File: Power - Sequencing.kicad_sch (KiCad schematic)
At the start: 0 parts

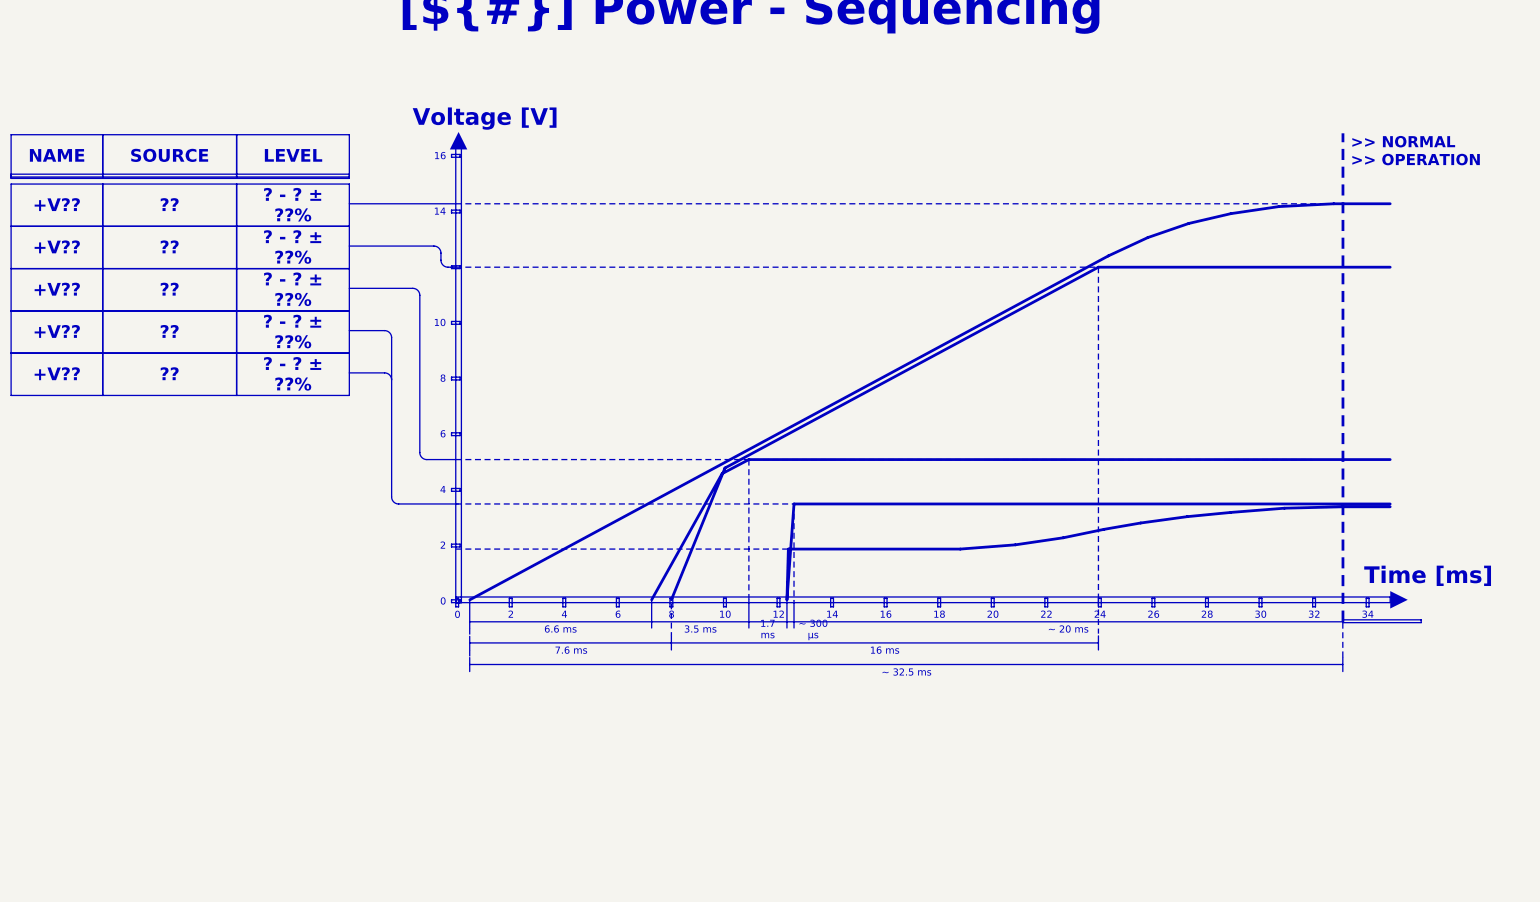
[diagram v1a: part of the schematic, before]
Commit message: Fill template pages: block diagram, power sequencing, cover notes, architecture
- Block Diagram redrawn from the real design: phase path (MR60PW, shunts),
  current and voltage channels with their gains and bandwidths, AD7606C-18,
  power chain, target specifications
- Power - Sequencing: start-up curves taken from the LTspice simulations
  (boost soft-start, analog rails) and rail table with sources, levels
  and timings
- Cover page: real design notes instead of the template examples
- Project Architecture: power-supply block documented, contiguous page
  numbers (Power Supply is page 6)
- Revision History: one column fed by the [Unreleased] changelog section
- sheet titles shortened so they fit the cover-page index: INA241 - Phase
  Sensing, Power Supply - Analog Rails

Sheet-level polylines carry no fill attribute (KiBot schematic reader).

Co-Authored-By: Claude Opus 5.5 <noreply@anthropic.com>
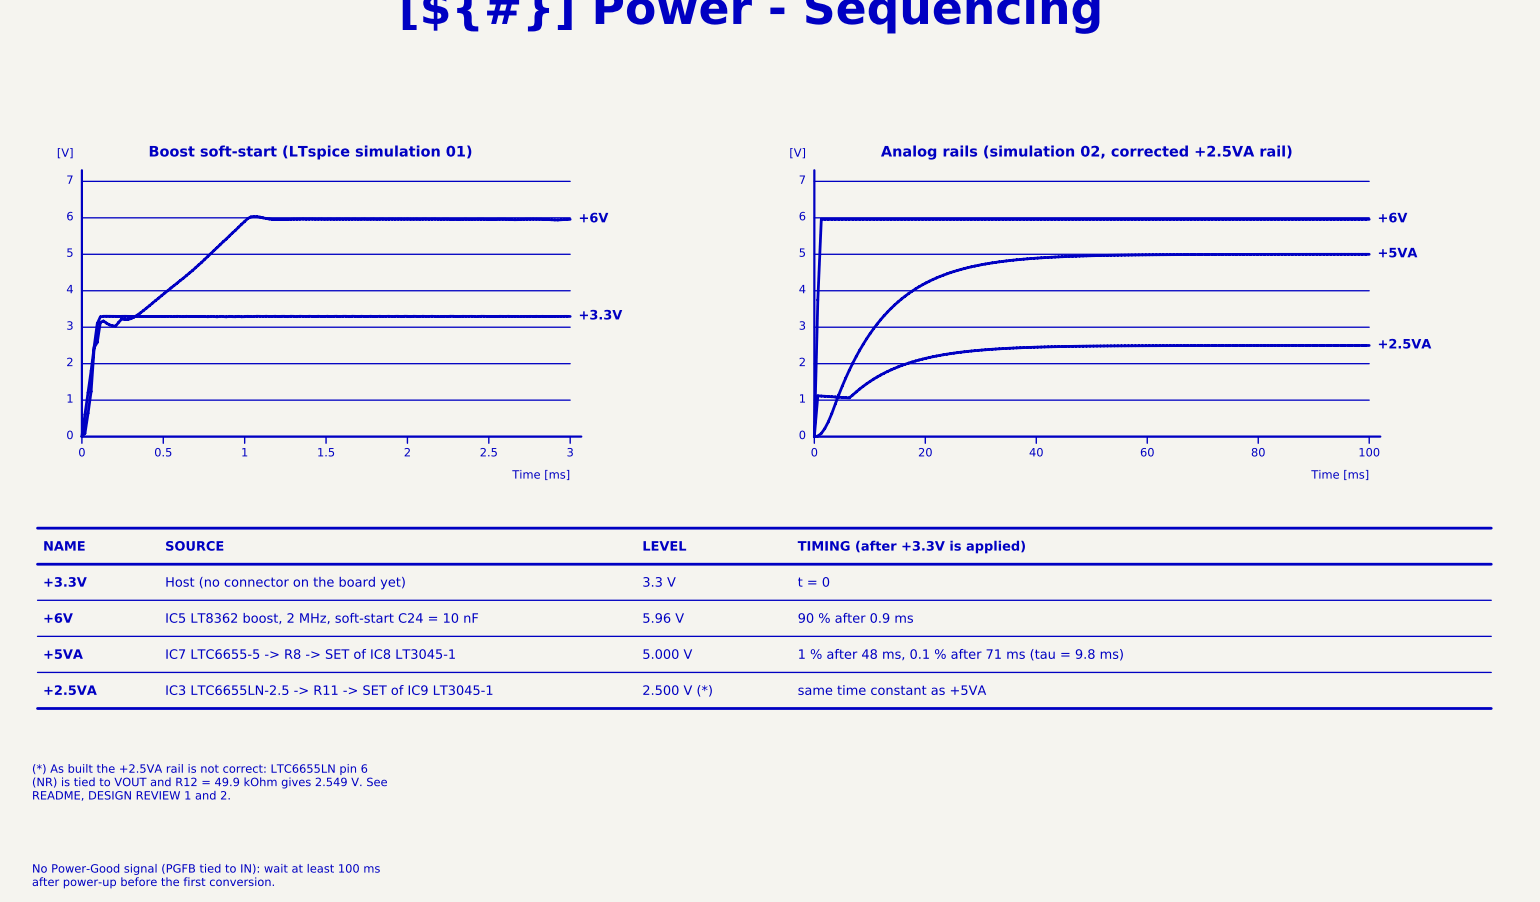
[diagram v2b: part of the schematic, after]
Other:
- note added: "+2.5VA"
- note added: "+3.3V"
- note added: "+5VA"
- note added: "+6V"
- note added: "0"
- note added: "0.5"
- note added: "1"
- note added: "1 % after 48 ms, 0.1 % after 71 ms (tau = 9.8 ms)"
- note added: "1.5"
- note added: "100"
- note added: "2"
- note added: "2.5"
- note added: "2.500 V (*)"
- note added: "20"
- note added: "3"
- note added: "3.3 V"
- note added: "4"
- note added: "40"
- note added: "5"
- note added: "5.000 V"
- note added: "5.96 V"
- note added: "6"
- note added: "60"
- note added: "7"
- note added: "80"
- note added: "90 % after 0.9 ms"
- note added: "Analog rails (simulation 02, corrected +2.5VA rail)"
- note added: "Boost soft-start (LTspice simulation 01)"
- note added: "Host (no connector on the board yet)"
- note added: "IC3 LTC6655LN-2.5 -> R11 -> SET of IC9 LT3045-1"
- note added: "IC5 LT8362 boost, 2 MHz, soft-start C24 = 10 nF"
- note added: "IC7 LTC6655-5 -> R8 -> SET of IC8 LT3045-1"
- note added: "LEVEL"
- note added: "NAME"
- note added: "SOURCE"
- note added: "TIMING (after +3.3V is applied)"
- note added: "[V]"
- note added: "same time constant as +5VA"
- note added: "t = 0"
- note removed: ">> NORMAL >> OPERATION"
- note removed: "Voltage [V]"

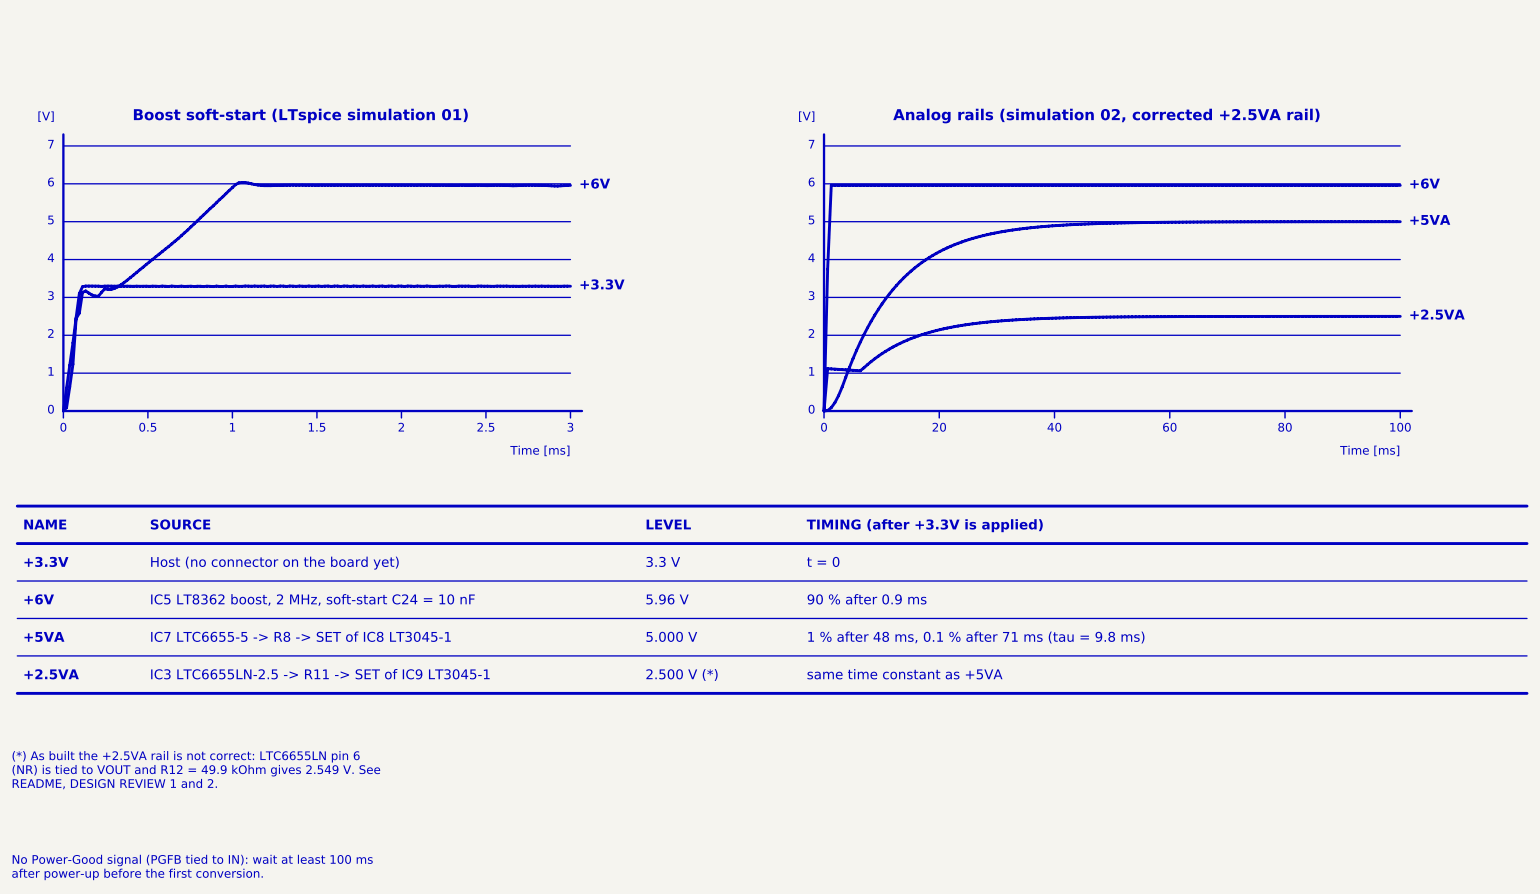
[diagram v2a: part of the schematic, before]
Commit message: Fix the +2.5VA reference, add XT60PW-M connectors, predict measurement quality
- IC3: LTC6655LN-2.5 replaced by the standard LTC6655-2.5, pin 6 is now
  VOUT_S tied to VOUT_F (the LN version has NR on that pin)
- R12: 49.9k -> 24.9k on the SET pin of IC9, +2.5VA = 2.500 V instead of
  2.549 V; both points removed from the README design review
- J5, J6: two Amass XT60PW-M added on the Connectors sheet and on the PCB,
  with symbol, footprint and 3D model in lib/. Their power pins are not
  wired yet
- Simulations 07 (ESC PWM waveforms through both channels) and 08 (Monte
  Carlo on the tolerances), analysed by measurement_quality.py into
  measurement_quality.md; plot style shared in plotstyle.py
- Simulations 01, 02, 04, results.md and their figures redone for the
  corrected rail
- README, README template and CHANGELOG updated; all sheets re-saved from
  KiCad

Co-Authored-By: Claude Opus 5.5 <noreply@anthropic.com>
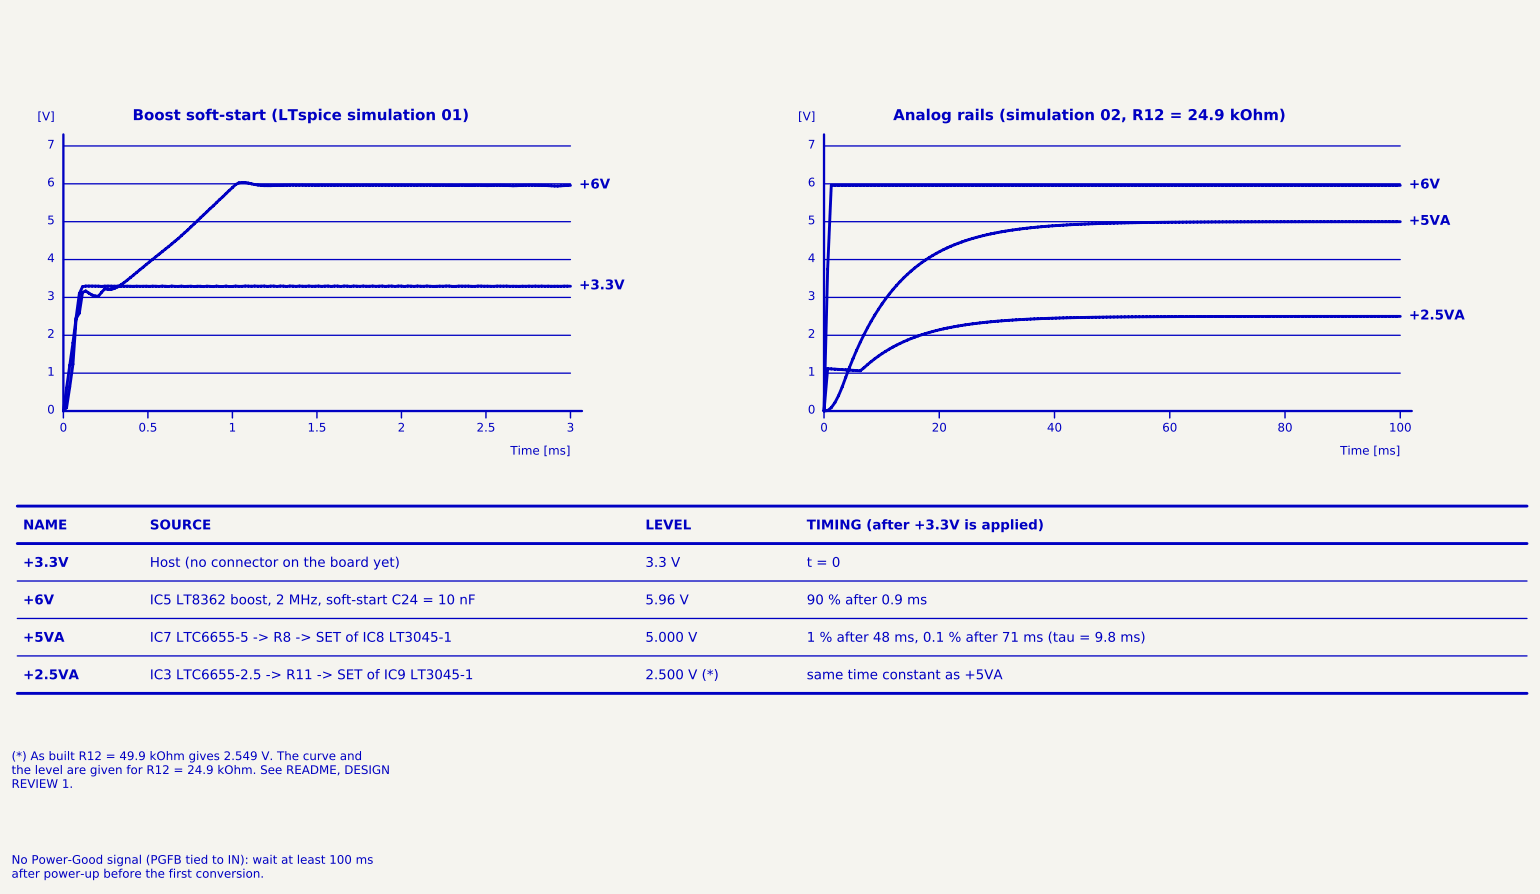
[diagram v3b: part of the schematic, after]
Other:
- note added: "Analog rails (simulation 02, R12 = 24.9 kOhm)"
- note added: "IC3 LTC6655-2.5 -> R11 -> SET of IC9 LT3045-1"
- note removed: "Analog rails (simulation 02, corrected +2.5VA rail)"
- note removed: "IC3 LTC6655LN-2.5 -> R11 -> SET of IC9 LT3045-1"
